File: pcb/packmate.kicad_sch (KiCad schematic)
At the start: 0 parts

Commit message: I think the pcb is pretty much done. Needs small things like test pads but it should at least work at this stage
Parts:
- added A1: RaspberryPi_Pico_W, Module:RaspberryPi_Pico_Common_THT, symbol MCU_Module:RaspberryPi_Pico_W_Extensive
- added BT1: Battery, symbol Device:Battery
- added BZ1: Buzzer, Buzzer_Beeper:Buzzer_12x9.5RM7.6, symbol Device:Buzzer
- added C1, C2: 0.1uf, Capacitor_SMD:C_01005_0402Metric, symbol Device:C
- added C3: 400uf, Capacitor_SMD:CP_Elec_3x5.3, symbol Device:C_Polarized
- added D5: Wireless In Use LED, LED_SMD:LED_0201_0603Metric, symbol Device:LED
- added Q1: 2N7002E, Package_TO_SOT_SMD:SOT-23, symbol Transistor_FET:2N7002E
- added R10: 20, Resistor_SMD:R_0201_0603Metric, symbol Device:R
- added R9: 10, Resistor_SMD:R_0201_0603Metric, symbol Device:R
- added SW2: Reset Button, Button_Switch_THT:SW_PUSH_6mm, symbol Switch:SW_Push
- added SW3: Left Button, Button_Switch_THT:SW_PUSH_6mm, symbol Switch:SW_Push
- added SW4: Right Button, Button_Switch_THT:SW_PUSH_6mm, symbol Switch:SW_Push
- added SW6: Wireless On/Off Switch, Button_Switch_THT:SW_E-Switch_EG1224_SPDT_Angled, symbol Switch:SW_SPST
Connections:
- new net: A1.27 (GPIO21), R9.1
- new net: D5.2 (A), R9.2
- new net: A1.20 (GPIO15), SW3.2
- new net: Q1.2 (S), R10.1
- new net: A1.9 (GPIO6), SW6.2 (B)
- new net: A1.16 (GPIO12), BZ1.1 (+)
- new net: A1.17 (GPIO13), Q1.1 (G)
- new net: A1.19 (GPIO14), SW4.2
- new net: A1.30 (RUN), SW2.2
- new net 3v3: A1.36 (3V3), C1.2, C2.2
- new net 5v: A1.39 (VSYS), C3.1
- new net Display Connector/CS: A1.12 (GPIO9)
- new net Display Connector/D/C: A1.11 (GPIO8)
- new net Display Connector/GND: A1.13 (GND), A1.18 (GND), A1.23 (GND), A1.28 (GND), A1.3 (GND), A1.38 (GND), A1.8 (GND), A1.D2 (GND), BZ1.2 (-), C1.1, C2.1, C3.2, D5.1 (K), Q1.3 (D), SW2.1, SW3.1, SW4.1, SW6.1 (A)
- new net Display Connector/LEDK: R10.2
- new net Display Connector/RST: A1.10 (GPIO7)
- new net Display Connector/SCL: A1.14 (GPIO10)
- new net Display Connector/SDA: A1.15 (GPIO11)
- new net LiPo Shim/+: BT1.1 (+)
- new net LiPo Shim/-: BT1.2 (-)
- new net LiPo Shim/3E: A1.37 (3V3_EN)
- new net LiPo Shim/VB: A1.40 (VBUS)
- new net MicroSD Card/CLK: A1.24 (GPIO18)
- new net MicroSD Card/CMD/SI: A1.25 (GPIO19)
- new net MicroSD Card/D0/SO: A1.21 (GPIO16)
- new net MicroSD Card/D3/CS: A1.22 (GPIO17)
- new net MicroSD Card/DET: A1.26 (GPIO20)
- new net RGB Matrix/Data: A1.7 (GPIO5)
- new net Trackball/BLU: A1.4 (GPIO2)
- new net Trackball/BTN: A1.6 (GPIO4)
- new net Trackball/DWN: A1.34 (GPIO28_ADC2)
- new net Trackball/GRN: A1.5 (GPIO3)
- new net Trackball/LFT: A1.32 (GPIO27_ADC1)
- new net Trackball/RED: A1.1 (GPIO0)
- new net Trackball/RHT: A1.31 (GPIO26_ADC0)
- new net Trackball/UP: A1.29 (GPIO22)
- new net Trackball/WHT: A1.2 (GPIO1)
- no-connect marks 0 -> 9
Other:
- added sheet Display Connector (st7789-connector.kicad_sch)
- added sheet LiPo Shim (lipo_shim.kicad_sch)
- added sheet MicroSD Card (sd_slot.kicad_sch)
- added sheet RGB Matrix (rgb_matrix.kicad_sch)
- added sheet Trackball (trackball.kicad_sch)

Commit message: Still tidying pcb design
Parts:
- removed C2: 0.1uf, Capacitor_SMD:C_01005_0402Metric, symbol Device:C
- added R13: 100, Resistor_SMD:R_0603_1608Metric, symbol Device:R
- C1: footprint Capacitor_SMD:C_01005_0402Metric -> Capacitor_SMD:C_0402_1005Metric
- C3: value 400uf -> 100uf; footprint Capacitor_SMD:CP_Elec_3x5.3 -> Capacitor_SMD:CP_Elec_4x5.4
- R10: footprint Resistor_SMD:R_0201_0603Metric -> Resistor_SMD:R_0603_1608Metric
- R9: value 10 -> 180; footprint Resistor_SMD:R_0201_0603Metric -> Resistor_SMD:R_0603_1608Metric
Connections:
- net Display Connector/GND: now also Q1.2 (S); no longer Q1.3 (D)
- net at R10.1: now also Q1.3 (D); no longer Q1.2 (S)
- net at A1.16 (GPIO12): now also R13.1; no longer BZ1.1 (+)
- net GND: now reaches A1.33 (AGND)
- net 3v3 renamed 3V3
- net 5v renamed VSYS
- new net: BZ1.1 (+), R13.2
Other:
- moved on the sheet: Q1
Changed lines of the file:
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@@
-	)
-	(junction
-		(at 240.03 113.03)
-		(diameter 0)
-		(color 0 0 0 0)
 	)
 	(junction
@@
 	)
 	(junction
-		(at 247.65 113.03)
-		(diameter 0)
-		(color 0 0 0 0)
-	)
-	(junction
 		(at 40.64 72.39)
 		(diameter 0)
@@
 	(wire
 		(pts
-			(xy 247.65 104.14) (xy 247.65 113.03)
+			(xy 247.65 104.14) (xy 247.65 140.97)
 		)
 		(stroke
@@
 	(wire
 		(pts
-			(xy 129.54 110.49) (xy 129.54 130.81)
+			(xy 129.54 110.49) (xy 129.54 123.19)
 		)
 		(stroke
@@
 	(wire
 		(pts
-			(xy 240.03 113.03) (xy 240.03 138.43)
-		)
-		(stroke
-			(width 0)
-			(type default)
-		)
-	)
-	(wire
-		(pts
 			(xy 124.46 29.21) (xy 121.92 29.21)
 		)
@@
 	(wire
 		(pts
-			(xy 240.03 96.52) (xy 240.03 113.03)
+			(xy 240.03 96.52) (xy 240.03 138.43)
 		)
 		(stroke
@@
 	(wire
 		(pts
-			(xy 247.65 113.03) (xy 247.65 140.97)
-		)
-		(stroke
-			(width 0)
-			(type default)
-		)
-	)
-	(wire
-		(pts
 			(xy 123.19 90.17) (xy 123.19 173.99)
 		)
@@
 		)
 	)
-	(label "5v"
+	(label "VSYS"
 		(at 149.86 29.21 0)
 		(effects
@@
 		)
 	)
-	(label "3v3"
+	(label "3V3"
 		(at 160.02 54.61 0)
 		(effects
@@
 			)
 		)
-		(property "Value" "10"
+		(property "Value" "180"
 			(at 198.12 102.87 90)
 			(show_name no)
@@
 			)
 		)
-		(property "Footprint" "Resistor_SMD:R_0201_0603Metric"
+		(property "Footprint" "Resistor_SMD:R_0603_1608Metric"
 			(at 198.12 104.648 90)
 			(hide yes)
@@
 				(path "/1b0954a2-3127-4772-a3bb-573d547242ae"
 					(reference "R9")
-					(unit 1)
-				)
-			)
-		)
-	)
-	(symbol
-		(lib_id "Device:C")
-		(at 243.84 113.03 270)
-		(unit 1)
-		(body_style 1)
-		(exclude_from_sim no)
-		(in_bom yes)
-		(on_board yes)
-		(in_pos_files yes)
-		(dnp no)
-		(fields_autoplaced yes)
-		(property "Reference" "C2"
-			(at 243.84 105.41 90)
-			(show_name no)
-			(do_not_autoplace no)
-			(effects
-				(font
-					(size 1.27 1.27)
-				)
-			)
-		)
-		(property "Value" "0.1uf"
-			(at 243.84 107.95 90)
-			(show_name no)
-			(do_not_autoplace no)
-			(effects
-				(font
-					(size 1.27 1.27)
-				)
-			)
-		)
-		(property "Footprint" "Capacitor_SMD:C_01005_0402Metric"
-			(at 240.03 113.9952 0)
-			(hide yes)
-			(show_name no)
-			(do_not_autoplace no)
-			(effects
-				(font
-					(size 1.27 1.27)
-				)
-			)
-		)
-		(property "Datasheet" ""
-			(at 243.84 113.03 0)
-			(hide yes)
-			(show_name no)
-			(do_not_autoplace no)
-			(effects
-				(font
-					(size 1.27 1.27)
-				)
-			)
-		)
-		(property "Description" "Unpolarized capacitor"
-			(at 243.84 113.03 0)
-			(hide yes)
-			(show_name no)
-			(do_not_autoplace no)
-			(effects
-				(font
-					(size 1.27 1.27)
-				)
-			)
-		)
-		(pin "1"
-		)
-		(pin "2"
-		)
-		(instances
-			(project "packmate"
-				(path "/1b0954a2-3127-4772-a3bb-573d547242ae"
-					(reference "C2")
 					(unit 1)
 				)
@@
 	)
 	(symbol
+		(lib_id "power:GND")
+		(at 177.8 118.11 90)
+		(unit 1)
+		(body_style 1)
+		(exclude_from_sim no)
+		(in_bom yes)
+		(on_board yes)
+		(in_pos_files yes)
+		(dnp no)
+		(property "Reference" "#PWR01"
+			(at 184.15 118.11 0)
+			(hide yes)
+			(show_name no)
+			(do_not_autoplace no)
+			(effects
+				(font
+					(size 1.27 1.27)
+				)
+			)
+		)
+		(property "Value" "GND"
+			(at 178.308 120.396 90)
+			(show_name no)
+			(do_not_autoplace no)
+			(effects
+				(font
+					(size 1.27 1.27)
+				)
+				(justify right)
+			)
+		)
+		(property "Footprint" ""
+			(at 177.8 118.11 0)
+			(hide yes)
+			(show_name no)
+			(do_not_autoplace no)
+			(effects
+				(font
+					(size 1.27 1.27)
+				)
+			)
+		)
+		(property "Datasheet" ""
+			(at 177.8 118.11 0)
+			(hide yes)
+			(show_name no)
+			(do_not_autoplace no)
+			(effects
+				(font
+					(size 1.27 1.27)
+				)
+			)
+		)
+		(property "Description" "Power symbol creates a global label with name \"GND\" , ground"
+			(at 177.8 118.11 0)
+			(hide yes)
+			(show_name no)
+			(do_not_autoplace no)
+			(effects
+				(font
+					(size 1.27 1.27)
+				)
+			)
+		)
+		(pin "1"
+		)
+		(instances
+			(project "packmate"
+				(path "/1b0954a2-3127-4772-a3bb-573d547242ae"
+					(reference "#PWR01")
+					(unit 1)
+				)
+			)
+		)
+	)
+	(symbol
 		(lib_id "Device:LED")
 		(at 207.01 102.87 180)
@@
 			)
 		)
-		(property "Footprint" "Resistor_SMD:R_0201_0603Metric"
+		(property "Footprint" "Resistor_SMD:R_0603_1608Metric"
 			(at 51.562 161.29 90)
 			(hide yes)
@@
 			)
 		)
-		(property "Footprint" "Capacitor_SMD:C_01005_0402Metric"
+		(property "Footprint" "Capacitor_SMD:C_0402_1005Metric"
 			(at 89.2048 163.83 0)
 			(hide yes)
@@
 	(symbol
 		(lib_id "Transistor_FET:2N7002E")
-		(at 58.42 152.4 270)
+		(at 58.42 152.4 90)
+		(mirror x)
 		(unit 1)
 		(body_style 1)
@@
 		(dnp no)
 		(property "Reference" "Q1"
-			(at 54.356 148.336 0)
+			(at 50.038 148.336 0)
 			(show_name no)
 			(do_not_autoplace no)
@@
 		)
 		(property "Value" "2N7002E"
-			(at 52.07 145.542 0)
+			(at 52.324 145.542 0)
 			(show_name no)
 			(do_not_autoplace no)
@@
 		)
 		(property "Footprint" "Package_TO_SOT_SMD:SOT-23"
-			(at 56.515 157.48 0)
+			(at 60.325 157.48 0)
 			(hide yes)
 			(show_name no)
@@
 		)
 		(property "Datasheet" "http://www.diodes.com/assets/Datasheets/ds30376.pdf"
-			(at 54.61 157.48 0)
+			(at 62.23 157.48 0)
 			(hide yes)
 			(show_name no)
@@
 	)
 	(symbol
+		(lib_id "Device:R")
+		(at 129.54 127 0)
+		(unit 1)
+		(body_style 1)
+		(exclude_from_sim no)
+		(in_bom yes)
+		(on_board yes)
+		(in_pos_files yes)
+		(dnp no)
+		(property "Reference" "R13"
+			(at 130.81 125.984 0)
+			(show_name no)
+			(do_not_autoplace no)
+			(effects
+				(font
+					(size 1.27 1.27)
+				)
+				(justify left)
+			)
+		)
+		(property "Value" "100"
+			(at 129.54 128.778 90)
+			(show_name no)
+			(do_not_autoplace no)
+			(effects
+				(font
+					(size 1.27 1.27)
+				)
+				(justify left)
+			)
+		)
+		(property "Footprint" "Resistor_SMD:R_0603_1608Metric"
+			(at 127.762 127 90)
+			(hide yes)
+			(show_name no)
+			(do_not_autoplace no)
+			(effects
+				(font
+					(size 1.27 1.27)
+				)
+			)
+		)
+		(property "Datasheet" ""
+			(at 129.54 127 0)
+			(hide yes)
+			(show_name no)
+			(do_not_autoplace no)
+			(effects
+				(font
+					(size 1.27 1.27)
+				)
+			)
+		)
+		(property "Description" "Resistor"
+			(at 129.54 127 0)
+			(hide yes)
+			(show_name no)
+			(do_not_autoplace no)
+			(effects
+				(font
+					(size 1.27 1.27)
+				)
+			)
+		)
+		(pin "2"
+		)
+		(pin "1"
+		)
+		(instances
+			(project "packmate"
+				(path "/1b0954a2-3127-4772-a3bb-573d547242ae"
+					(reference "R13")
+					(unit 1)
+				)
+			)
+		)
+	)
+	(symbol
 		(lib_id "Switch:SW_Push")
 		(at 101.6 134.62 0)
@@
 		(dnp no)
 		(property "Reference" "C3"
-			(at 13.716 52.832 0)
+			(at 18.796 53.594 0)
 			(show_name no)
 			(do_not_autoplace no)
@@
 			)
 		)
-		(property "Value" "400uf"
-			(at 13.716 55.372 0)
+		(property "Value" "100uf"
+			(at 18.796 56.134 0)
 			(show_name no)
 			(do_not_autoplace no)
@@
 			)
 		)
-		(property "Footprint" "Capacitor_SMD:CP_Elec_3x5.3"
+		(property "Footprint" "Capacitor_SMD:CP_Elec_4x5.4"
 			(at 28.9052 58.42 0)
 			(hide yes)

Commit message: Still improving pcb, I learned what a fiducial is today
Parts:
- removed C1: 0.1uf, Capacitor_SMD:C_0402_1005Metric, symbol Device:C
- removed C3: 100uf, Capacitor_SMD:CP_Elec_4x5.4, symbol Device:C_Polarized
- removed Q1: 2N7002E, Package_TO_SOT_SMD:SOT-23, symbol Transistor_FET:2N7002E
- removed R10: 20, Resistor_SMD:R_0603_1608Metric, symbol Device:R
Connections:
- net Display Connector/GND is gone; now on net GND: A1.13 (GND), A1.18 (GND), A1.23 (GND), A1.28 (GND), A1.3 (GND), A1.38 (GND), A1.8 (GND), A1.D2 (GND), BZ1.2 (-), D5.1 (K), SW2.1, SW3.1, SW4.1, SW6.1 (A)
- net Display Connector/LEDK: now also A1.17 (GPIO13)
- net 3V3 renamed +3.3V
- no-connect marks 9 -> 8
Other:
- sheet Display Connector ports: added none; removed GND, LEDA, VDD
- sheet LiPo Shim ports: added none; removed GND
- sheet MicroSD Card ports: added none; removed 3V, GND
- sheet RGB Matrix ports: added none; removed 3-5V, GND
- sheet Trackball ports: added none; removed +3v3, GND
- moved on the sheet: BT1, BZ1, SW6

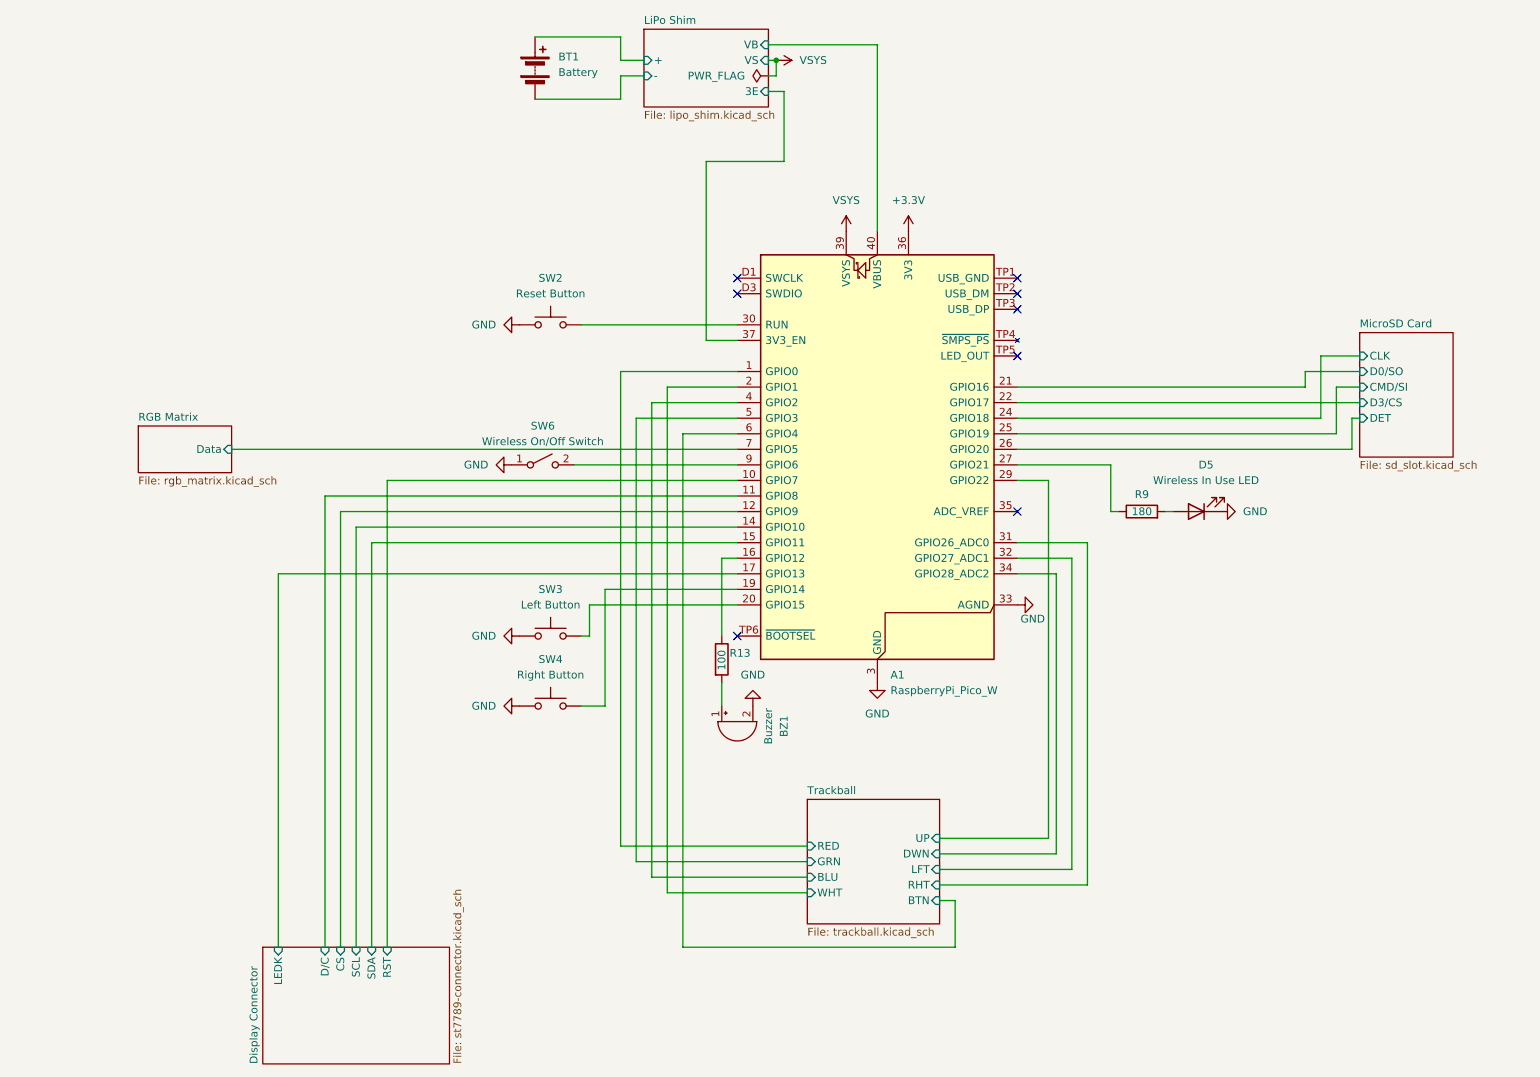
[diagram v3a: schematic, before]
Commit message: I think the PCB is almost done for real this time chat. Just gotta add part numbers for the BOM
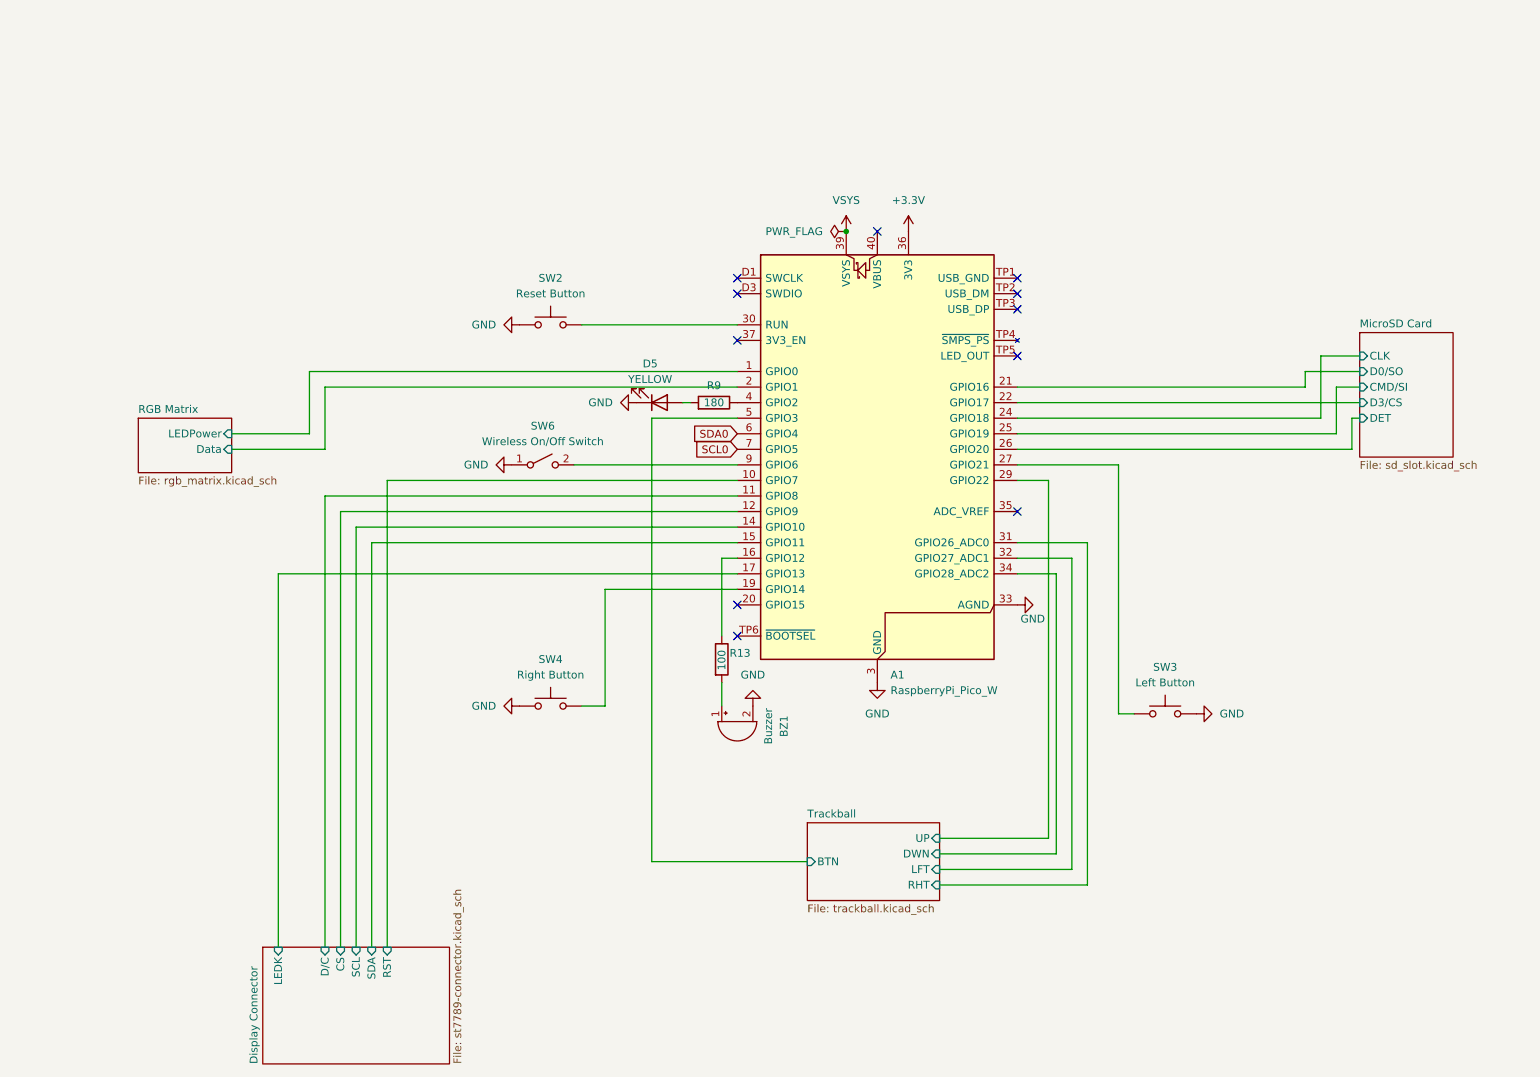
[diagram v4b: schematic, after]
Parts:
- removed BT1: Battery, symbol Device:Battery
- D5: value Wireless In Use LED -> YELLOW
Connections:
- net Trackball/BLU is gone; now on an unnamed net: A1.4 (GPIO2)
- net Trackball/GRN is gone; now on net Trackball/BTN: A1.5 (GPIO3)
- net Trackball/WHT is gone; now on net RGB Matrix/Data: A1.2 (GPIO1)
- net RGB Matrix/Data: no longer A1.7 (GPIO5)
- net Trackball/BTN: no longer A1.6 (GPIO4)
- net at R9.1: no longer A1.27 (GPIO21)
- net at SW3.2: now also A1.27 (GPIO21); no longer A1.20 (GPIO15)
- net LiPo Shim/3E: no longer names the net of A1.37 (3V3_EN)
- net LiPo Shim/VB: no longer names the net of A1.40 (VBUS)
- net Trackball/RED renamed RGB Matrix/LEDPower
- new net SCL0: A1.7 (GPIO5)
- new net SDA0: A1.6 (GPIO4)
- no-connect marks 8 -> 11
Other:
- removed sheet LiPo Shim
- sheet RGB Matrix ports: added LEDPower; removed none
- sheet Trackball ports: added none; removed BLU, GRN, RED, WHT
- moved on the sheet: D5, R9, SW3

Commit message: I think the PCB is ready to ship, just gonna tidy up a couple more things
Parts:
- A1: now not fitted
- BZ1: footprint Buzzer_Beeper:Buzzer_12x9.5RM7.6 -> Buzzer_Beeper:Buzzer_TDK_PS1240P02BT_D12.2mm_H6.5mm; MPN (none) -> PS1240P02BT; Manufacturer (none) -> TDK; SilkLabel (none) -> PIEZO; now not fitted
- D5: footprint LED_SMD:LED_0201_0603Metric -> LED_SMD:LED_0402_1005Metric; MPN (none) -> APHHS1005SYCK; Manufacturer (none) -> Kingbright; SilkLabel (none) -> WIRELESS IND.
- R13: MPN (none) -> ERJ-3EKF1000V; Manufacturer (none) -> Panasonic Industry
- R9: MPN (none) -> CRGCQ0603F180R; Manufacturer (none) -> TE Connectivity Passive Product
- SW2: MPN (none) -> B3F-1000; Manufacturer (none) -> Aratas (Formerly Omron Components); SilkLabel (none) -> RESET; now not fitted
- SW3: MPN (none) -> B3F-1000; Manufacturer (none) -> Aratas (Formerly Omron Components); SilkLabel (none) -> LEFT; now not fitted
- SW4: MPN (none) -> B3F-1000; Manufacturer (none) -> Aratas (Formerly Omron Components); SilkLabel (none) -> RIGHT; now not fitted
- SW6: MPN (none) -> EG1224; Manufacturer (none) -> E-Switch; SilkLabel (none) -> WIRELESS SW; now not fitted
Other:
- sheet Trackball ports: added SCL, SDA; removed none
